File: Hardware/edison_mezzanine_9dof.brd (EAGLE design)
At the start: 30.5 x 44.5 mm, 41 parts, among them U1 LSM9DS0, U2 EDISON_CONNECTOR_FULLMOUNTING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, U3 EDISON_CONNECTOR_FULLHEADER

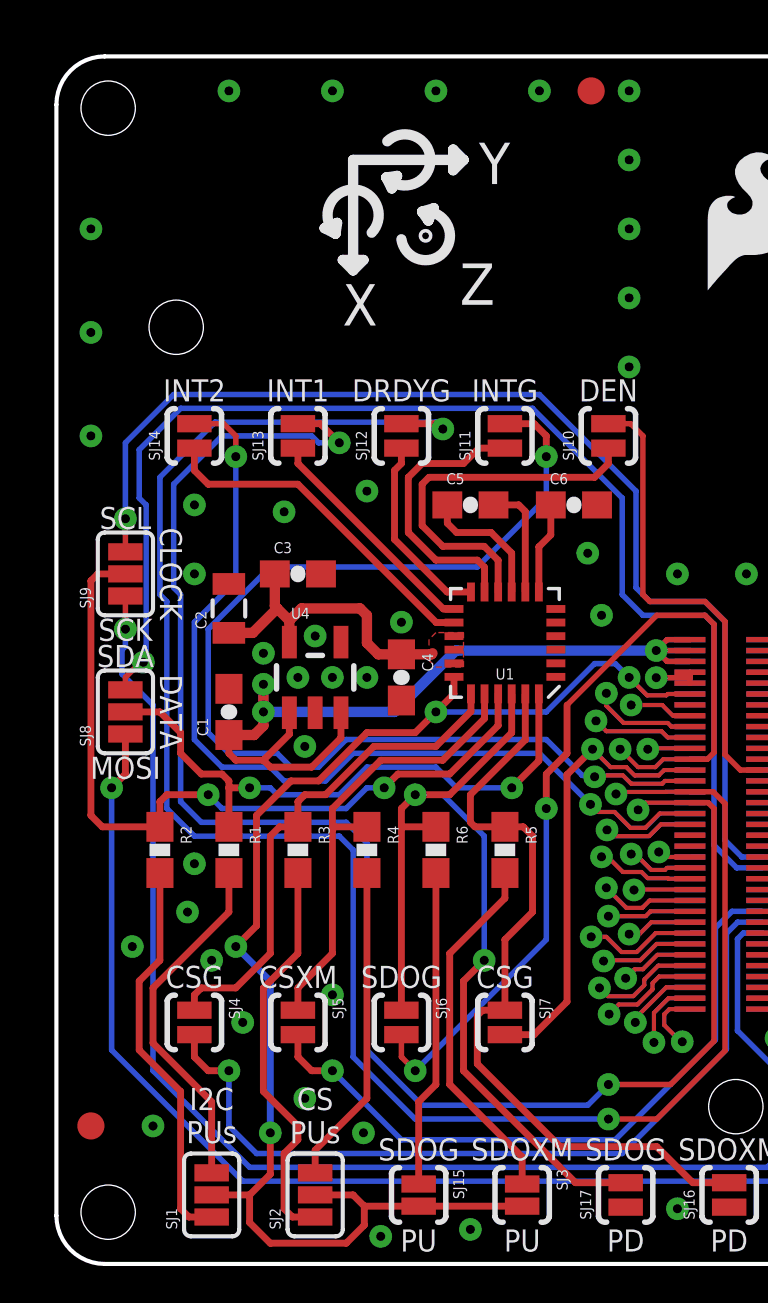
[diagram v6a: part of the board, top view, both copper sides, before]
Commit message: Added second side fiducials.
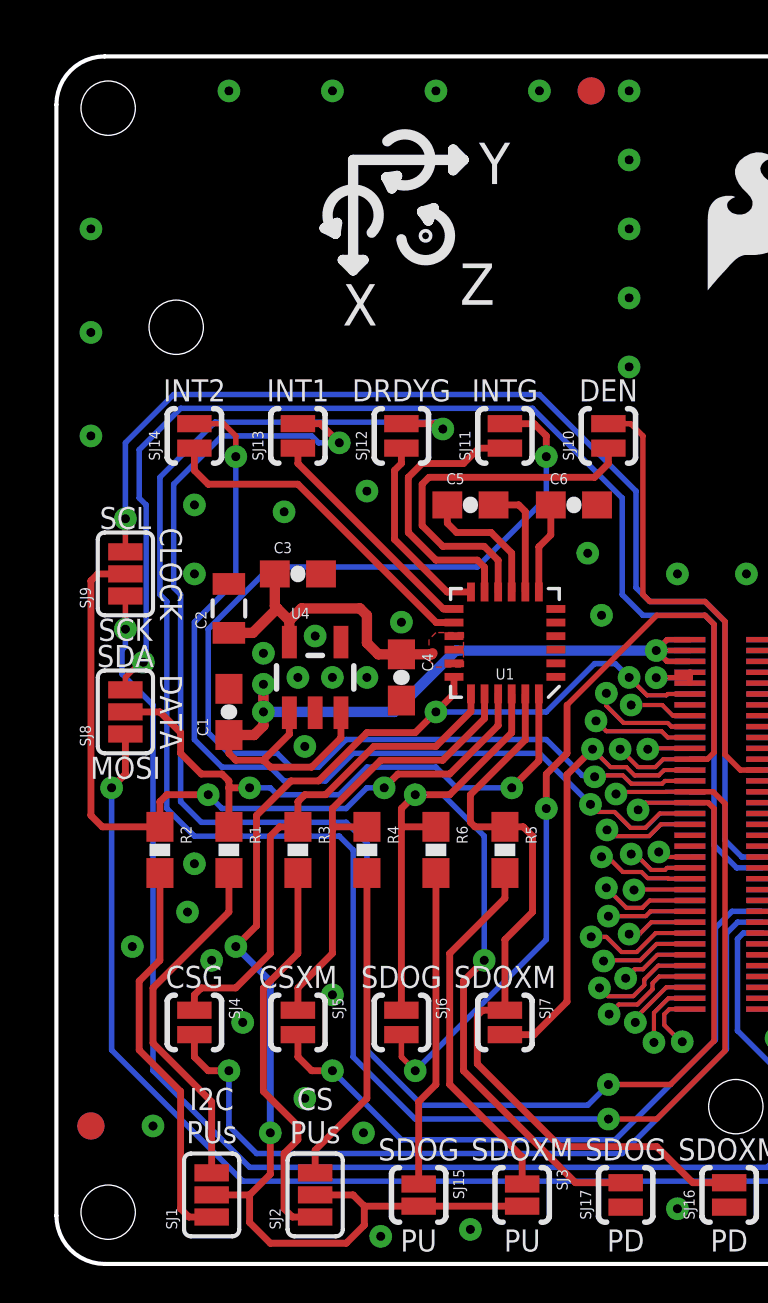
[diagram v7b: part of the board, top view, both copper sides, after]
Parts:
- added FID3, FID4: FIDUCIAL1X2, SparkFun-Aesthetics:FIDUCIAL-1X2
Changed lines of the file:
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@@
 <layer number="2" name="Route2" color="1" fill="3" visible="no" active="yes"/>
 <layer number="15" name="Route15" color="4" fill="6" visible="no" active="yes"/>
-<layer number="16" name="Bottom" color="1" fill="1" visible="yes" active="yes"/>
+<layer number="16" name="Bottom" color="1" fill="1" visible="no" active="yes"/>
 <layer number="17" name="Pads" color="2" fill="1" visible="yes" active="yes"/>
 <layer number="18" name="Vias" color="2" fill="1" visible="yes" active="yes"/>
@@
 <layer number="20" name="Dimension" color="15" fill="1" visible="yes" active="yes"/>
 <layer number="21" name="tPlace" color="16" fill="1" visible="yes" active="yes"/>
-<layer number="22" name="bPlace" color="14" fill="1" visible="yes" active="yes"/>
+<layer number="22" name="bPlace" color="14" fill="1" visible="no" active="yes"/>
 <layer number="23" name="tOrigins" color="15" fill="1" visible="yes" active="yes"/>
-<layer number="24" name="bOrigins" color="15" fill="1" visible="yes" active="yes"/>
+<layer number="24" name="bOrigins" color="15" fill="1" visible="no" active="yes"/>
 <layer number="25" name="tNames" color="7" fill="1" visible="no" active="yes"/>
 <layer number="26" name="bNames" color="7" fill="1" visible="no" active="yes"/>
@@
 <layer number="43" name="vRestrict" color="2" fill="10" visible="no" active="yes"/>
 <layer number="44" name="Drills" color="7" fill="1" visible="no" active="yes"/>
-<layer number="45" name="Holes" color="7" fill="1" visible="yes" active="yes"/>
+<layer number="45" name="Holes" color="7" fill="1" visible="no" active="yes"/>
 <layer number="46" name="Milling" color="3" fill="1" visible="no" active="yes"/>
-<layer number="51" name="tDocu" color="6" fill="1" visible="yes" active="yes"/>
+<layer number="51" name="tDocu" color="6" fill="1" visible="no" active="yes"/>
 <layer number="52" name="bDocu" color="7" fill="1" visible="no" active="yes"/>
 <layer number="3" name="Route3" color="4" fill="3" visible="no" active="no"/>
@@
 <wire x1="28.702" y1="0" x2="1.778" y2="0" width="0.1524" layer="20"/>
 <wire x1="0" y1="1.778" x2="0" y2="42.672" width="0.1524" layer="20"/>
-<text x="21.59" y="-20.32" size="1.6764" layer="51" ratio="15">Shawn Hymel</text>
+<text x="17.78" y="-20.32" size="1.6764" layer="51" ratio="15">Shawn Hymel</text>
 <hole x="28.575" y="1.905" drill="2"/>
 <hole x="1.905" y="1.905" drill="2"/>
@@
 <text x="8.89" y="10.16" size="0.8128" layer="21" font="vector" ratio="15" align="bottom-center">CSXM</text>
 <text x="12.7" y="10.16" size="0.8128" layer="21" font="vector" ratio="15" align="bottom-center">SDOG</text>
-<text x="16.51" y="10.16" size="0.8128" layer="21" font="vector" ratio="15" align="bottom-center">CSG</text>
+<text x="16.51" y="10.16" size="0.8128" layer="21" font="vector" ratio="15" align="bottom-center">SDOXM</text>
 <text x="2.54" y="21.971" size="0.8128" layer="21" font="vector" ratio="15" align="bottom-center">SDA</text>
 <text x="2.54" y="27.051" size="0.8128" layer="21" font="vector" ratio="15" align="bottom-center">SCL</text>
@@
 <element name="SJ16" library="SparkFun-Passives" package="PAD-JUMPER-2-NO_YES_SILK" value="JUMPER-PAD-2-NOYES_SILK" x="24.765" y="2.54" rot="R90"/>
 <element name="SJ17" library="SparkFun-Passives" package="PAD-JUMPER-2-NO_YES_SILK" value="JUMPER-PAD-2-NOYES_SILK" x="20.955" y="2.54" rot="R90"/>
+<element name="FID3" library="SparkFun-Aesthetics" package="FIDUCIAL-1X2" value="FIDUCIAL1X2" x="19.685" y="43.18" rot="MR0"/>
+<element name="FID4" library="SparkFun-Aesthetics" package="FIDUCIAL-1X2" value="FIDUCIAL1X2" x="1.27" y="5.08" rot="MR0"/>
 </elements>
 <signals>

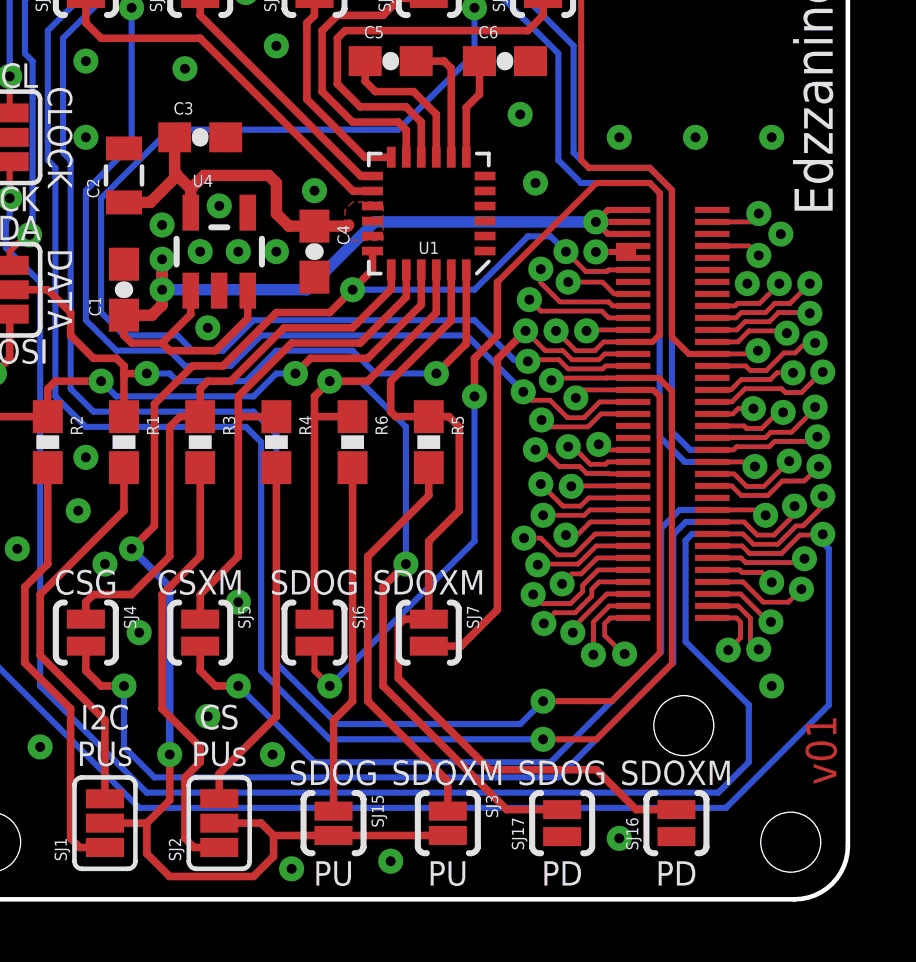
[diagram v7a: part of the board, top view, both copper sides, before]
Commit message: Connected SDO_XM and SDO_G together to SPI2_RX on Edison.
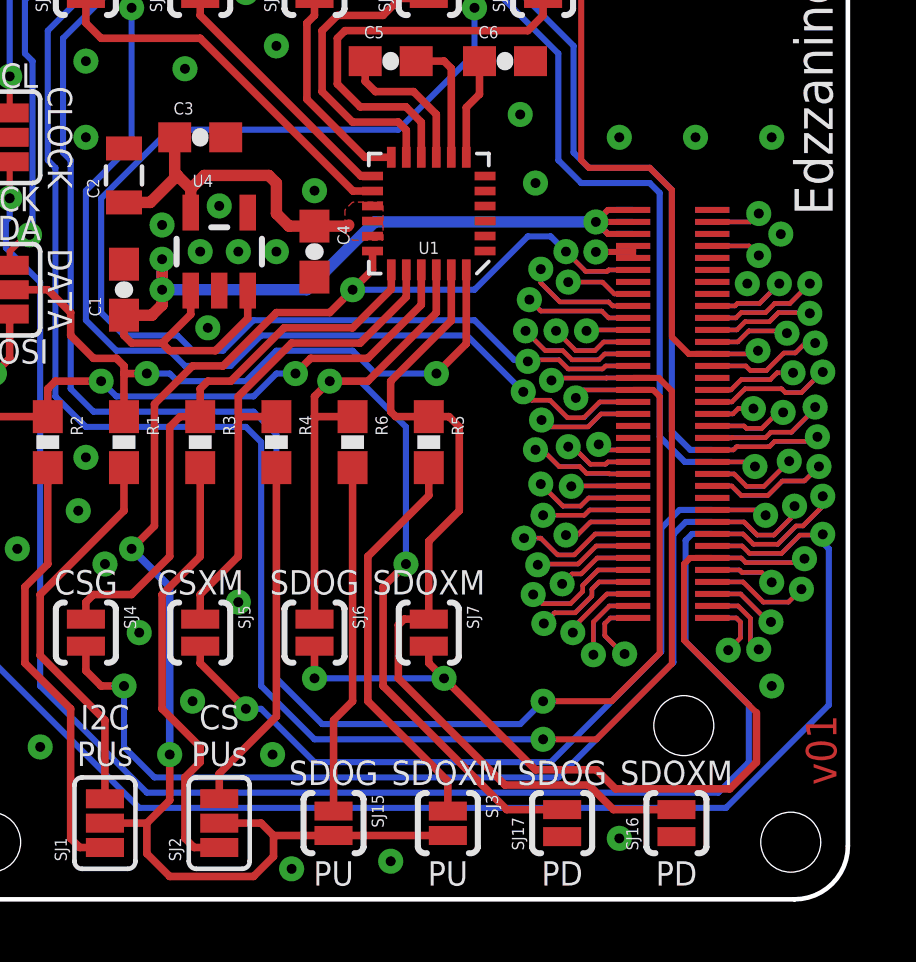
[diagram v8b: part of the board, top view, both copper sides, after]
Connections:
- net GP114_SPI_2_RXD: now also SJ6.2, SJ7.2
- net GP44: no longer SJ6.2
- net GP45: no longer SJ7.2
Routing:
- net GP44: track 35.9 -> 5.93 mm, vias 3 -> 1
- net GP114_SPI_2_RXD: track 6.38 -> 34.0 mm, vias 1 -> 3
- net GP45: track 20.6 -> 8.13 mm
